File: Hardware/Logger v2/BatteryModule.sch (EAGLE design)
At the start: 23 parts, among them J2 5.5x2.1mm Barrel, J3 5.5x2.1mm Barrel, J4 5.5x2.1mm Barrel, J5 5.5x2.1mm Barrel

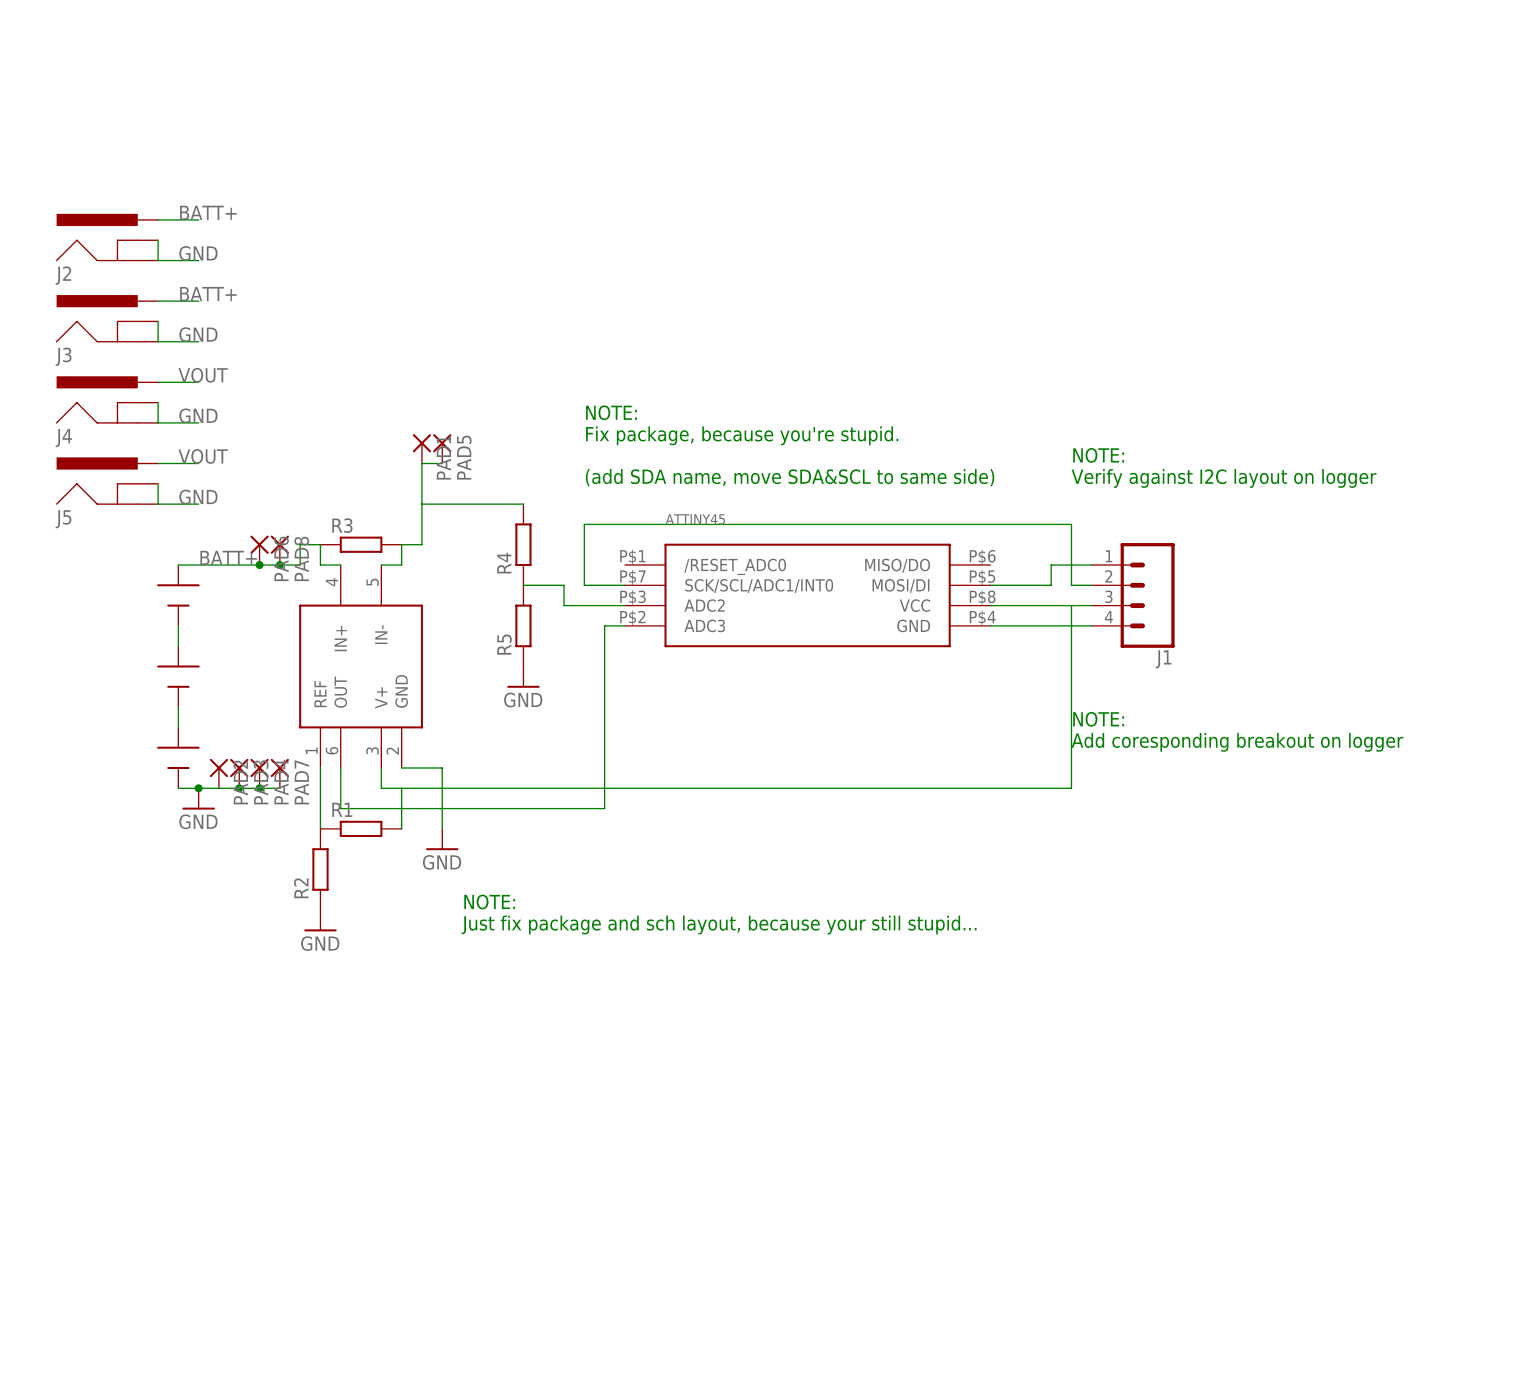
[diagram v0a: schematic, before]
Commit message: Added complete battery board schematic
Added a complete and functional schematic for the battery board, revisions still pending should be functional
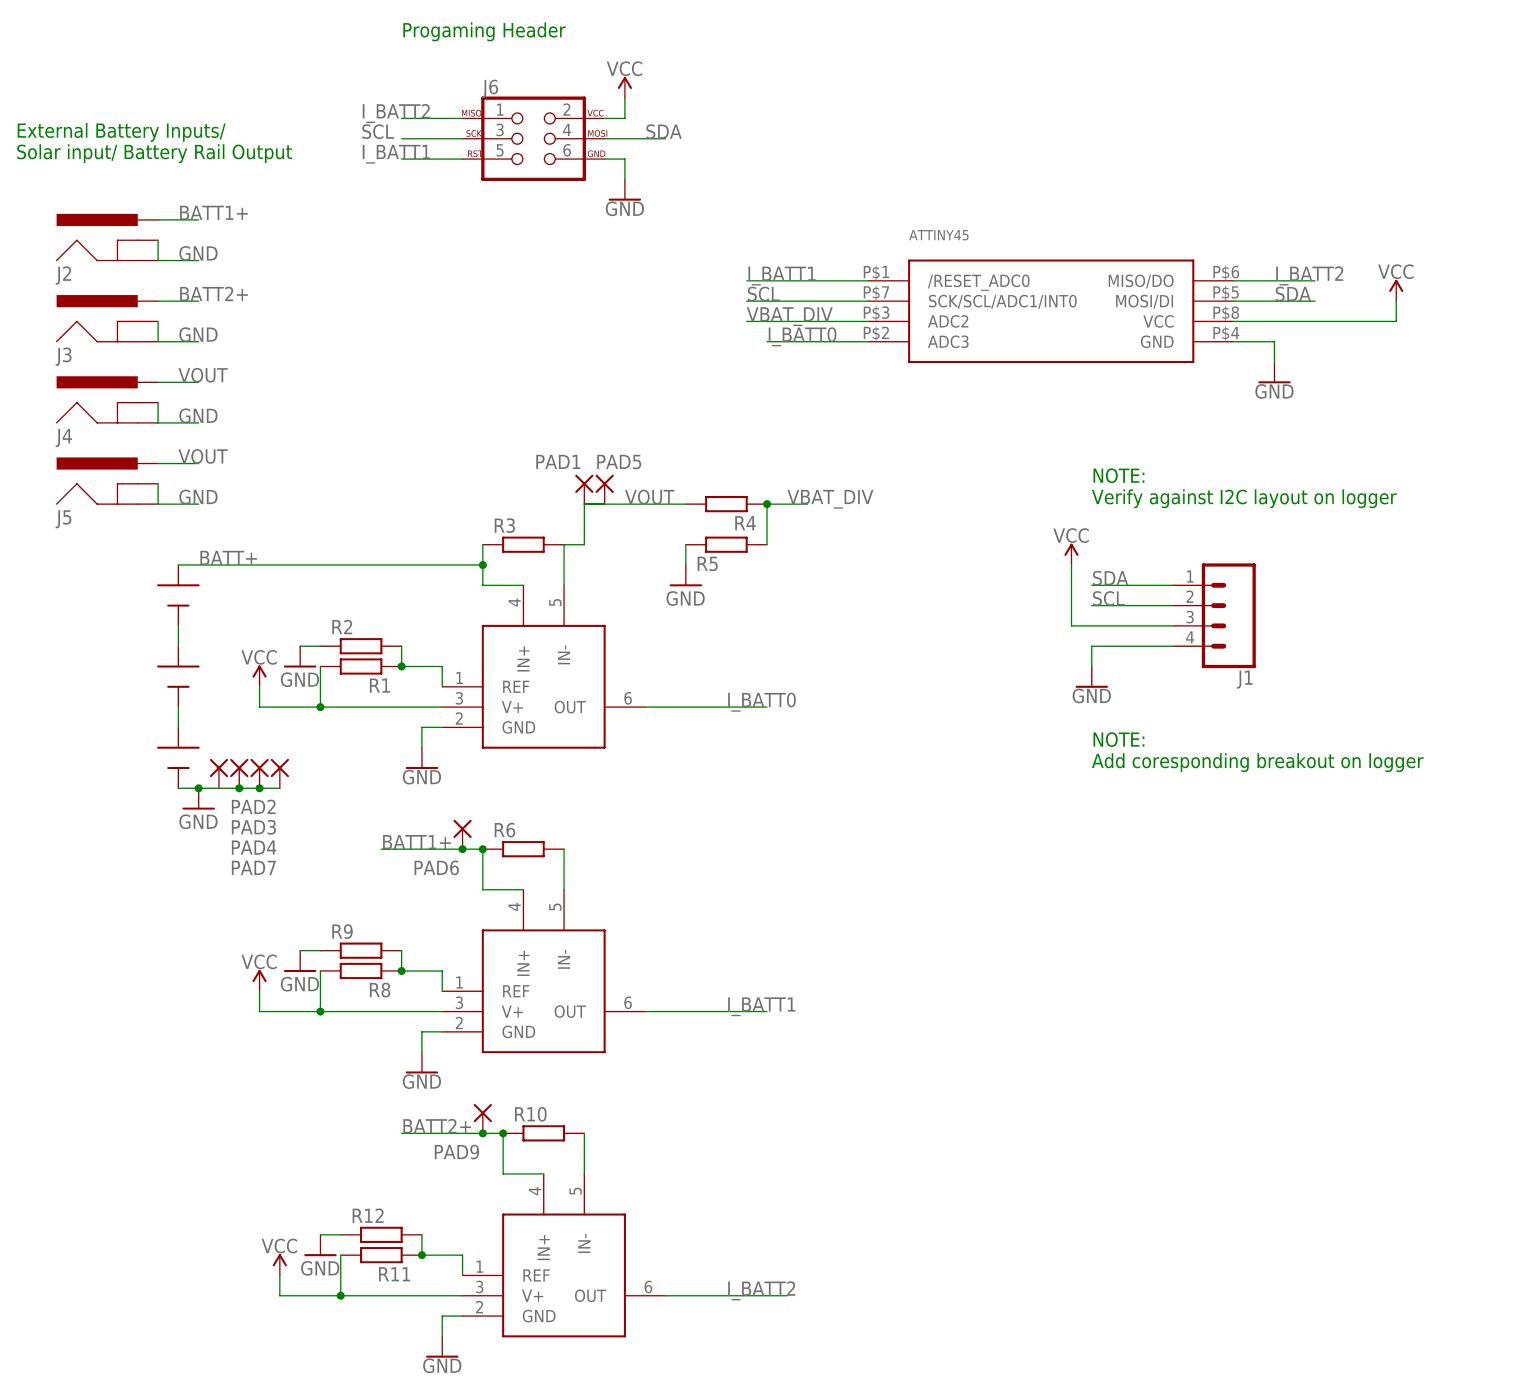
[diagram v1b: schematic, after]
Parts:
- removed PAD8: (no value), wirepad:2,15/1,0
- added J6: AVR_SPI_PROG_3X2PTH, SparkFun-Connectors:AVR_SPI_PROG_3X2PTH
- added PAD9: (no value), wirepad:2,15/1,0
- added R10, R6: (no value), rcl:R-EU_R0805
- added R11, R12, R8, R9: (no value), rcl:R-EU_R0603
- added U$6, U$8: INA212, texas:INA212
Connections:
- net N$11 renamed VBAT_DIV
- net N$8 renamed I_BATT0
- new net BATT1+: J2.PWR, PAD6.P, R6.1, U$6.IN+
- new net BATT2+: J3.PWR, PAD9.P, R10.1, U$8.IN+
- new net I_BATT1: J6.5, U$4./RESET_ADC0, U$6.OUT
- new net I_BATT2: J6.1, U$4.MISO/DO, U$8.OUT
- new net SCL: J1.2, J6.3, U$4.SCK/SCL/ADC1/INT0
- new net SDA: J1.1, J6.4, U$4.MOSI/DI
- new net VCC: J1.3, J6.2, R1.2, R11.2, R8.2, U$4.VCC, U$5.V+, U$8.V+
- net BATT+: no longer J2.PWR, J3.PWR, PAD6.P, PAD8.P
- net GND: now also J1.4, J6.6, R12.1, R9.1, U$4.GND, U$8.GND
- net N$3: now also R8.1, R9.2, U$6.REF; no longer J1.1, U$4.MOSI/DI
- net N$4: now also R6.2, U$6.IN-; no longer J1.2, U$4.SCK/SCL/ADC1/INT0
- net N$5: now also R10.2, U$8.IN-; no longer J1.3, R1.2, U$4.VCC, U$5.V+
- net N$6: now also R11.1, R12.2, U$8.REF; no longer J1.4, U$4.GND
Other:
- note added: "External Battery Inputs/ Solar input/ Battery Rail Output"
- note added: "Progaming Header"
- note removed: "NOTE: Fix package, because you're stupid. (add SDA name, move SDA&SCL to same side)"
- note removed: "NOTE: Just fix package and sch layout, because your still stupid..."
- moved on the sheet: J1, PAD1, PAD5, PAD6, R1, R2, R3, R4, R5
